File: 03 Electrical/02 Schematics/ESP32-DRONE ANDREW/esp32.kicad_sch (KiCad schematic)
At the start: 1 part, among them U1 ESP32-C3

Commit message: finished power managemnt
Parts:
- removed U1: ESP32-C3, Package_DFN_QFN:QFN-32-1EP_5x5mm_P0.5mm_EP3.7x3.7mm, symbol MCU_Espressif:ESP32-C3
- added C21: 1u, symbol Device:C_Small
- added L5: 39n, symbol Device:L_Small
- added P?: USB_C_Plug, symbol Connector:USB_C_Plug
- added R11: 0R0, symbol Device:R_Small
- added U5: ~, symbol Library 1:ESP32-PICO-V3
- added U?: CH340G, Package_SO:SOIC-16_3.9x9.9mm_P1.27mm, symbol Interface_USB:CH340G
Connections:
- new net: P?.A4 (VBUS), P?.A9 (VBUS), P?.B4 (VBUS), P?.B9 (VBUS)
- new net: P?.S1 (SHIELD), R11.1
- new net +3.3V: L5.1, U5.3 (VDDA3P3), U5.4 (VDDA3P3)
- new net GND1: C21.2, P?.A1 (GND), P?.A12 (GND), P?.B1 (GND), P?.B12 (GND), R11.2, U5.49 (GND)
- new net VDDA: C21.1, L5.2, U5.1 (VDDA), U5.46 (VDDA)
- no-connect marks 1 -> 4
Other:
- note removed: "No antenna required for the ESP32 will be using the LoRA module to communicate with our system"

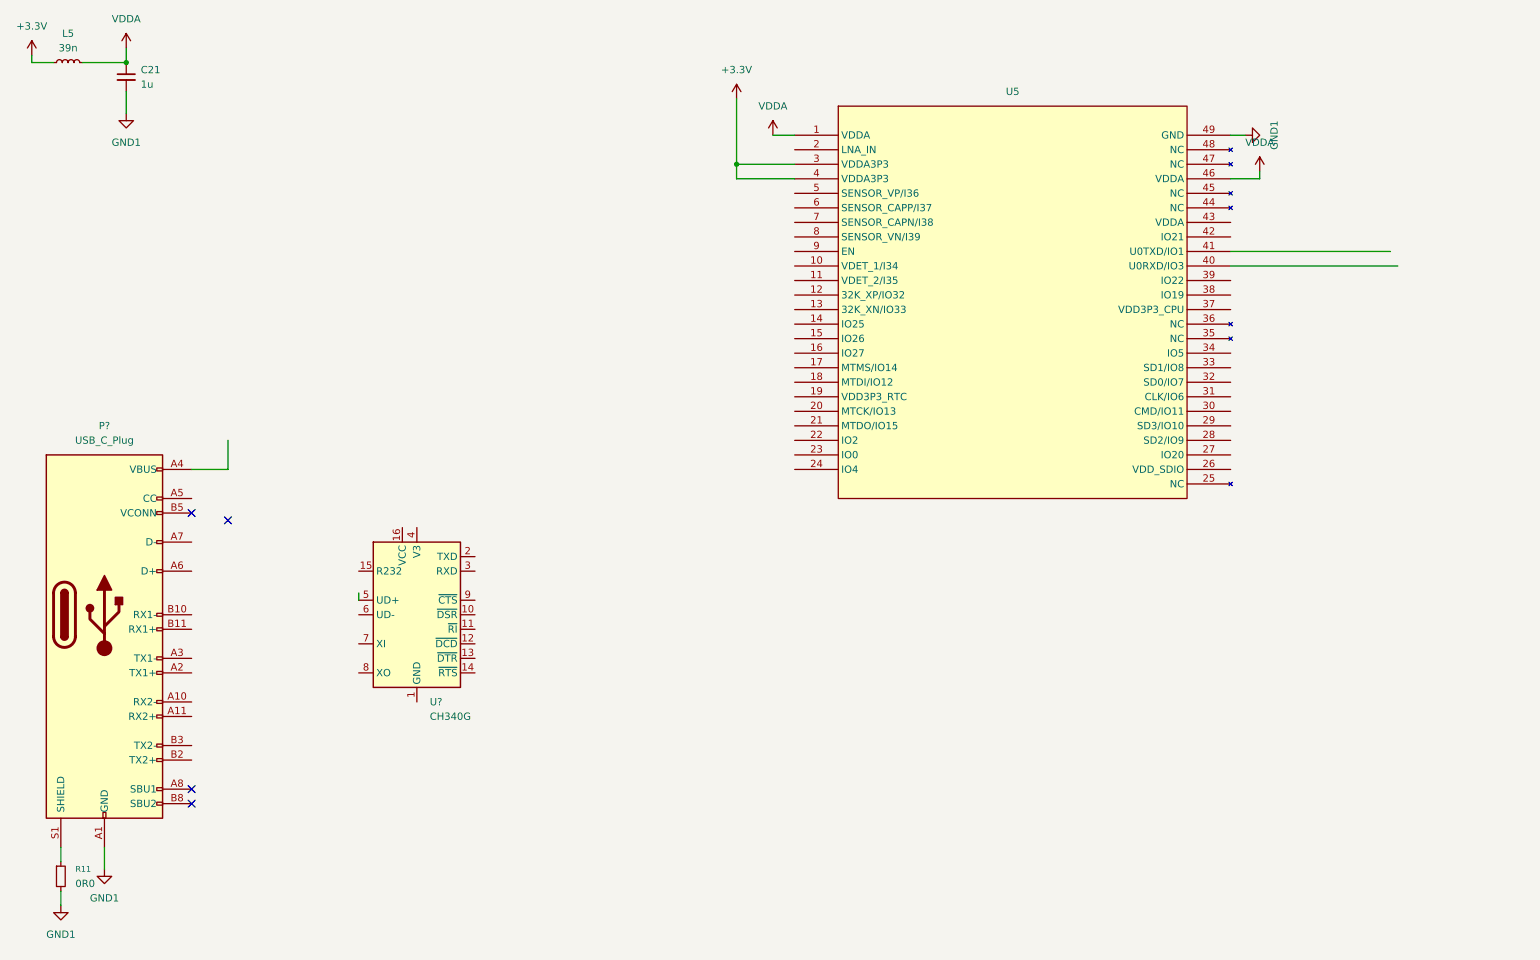
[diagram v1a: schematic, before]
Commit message: update 6/11
added the debugger circuit for the esp32 :
still missing the GPS circuit and the RF circuit
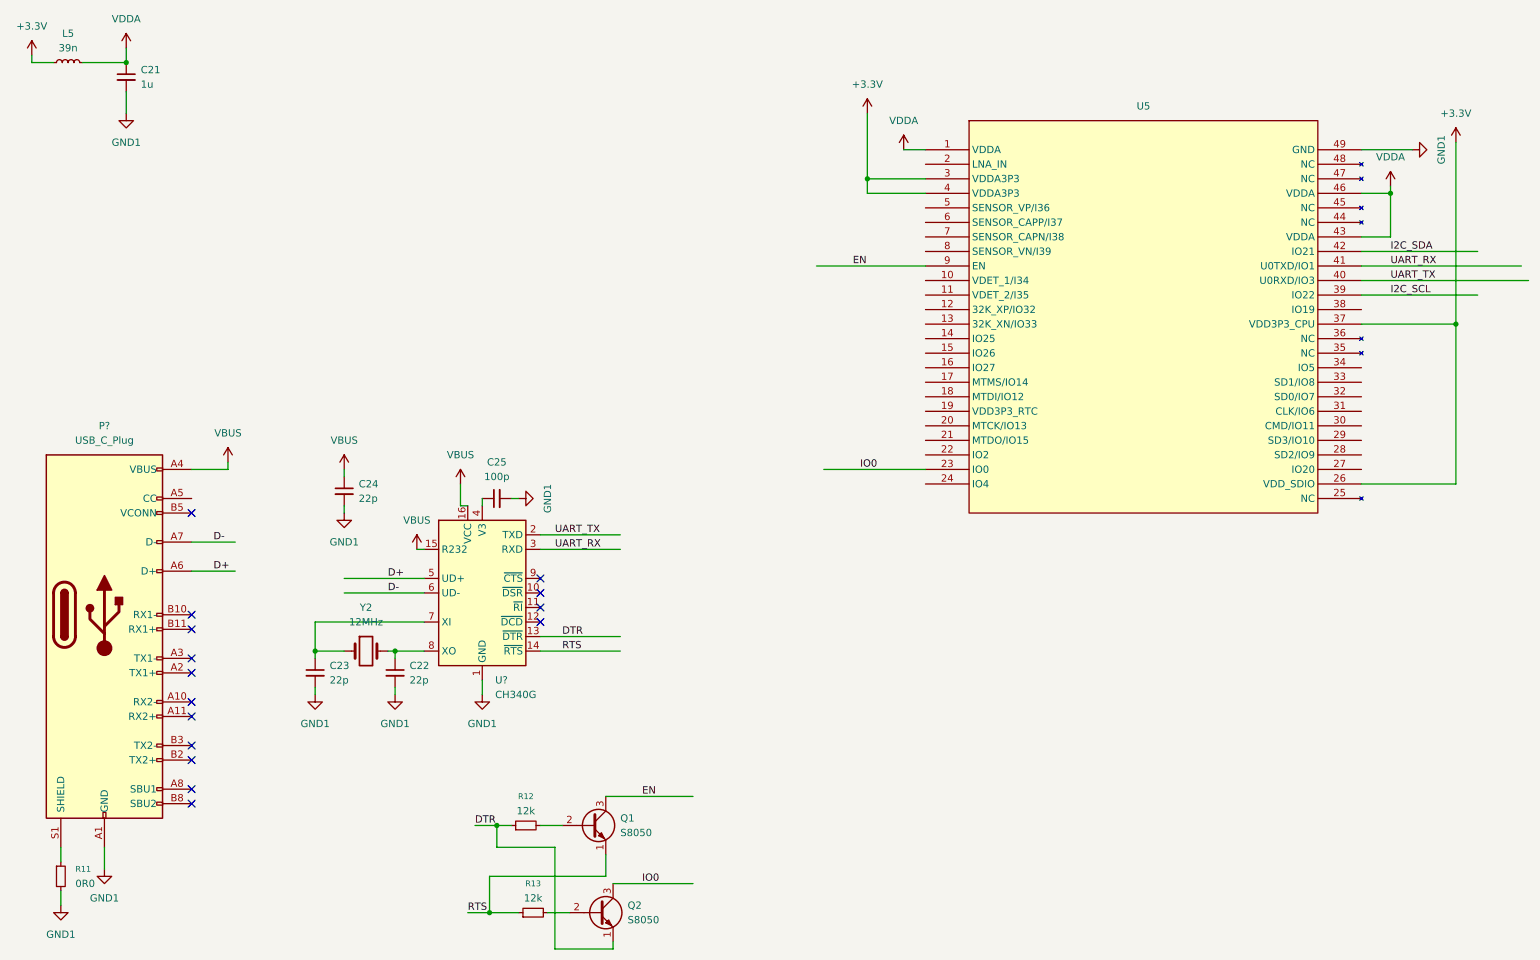
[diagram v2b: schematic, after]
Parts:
- added C22, C23, C24: 22p, symbol Device:C_Small
- added C25: 100p, symbol Device:C_Small
- added Q1, Q2: S8050, Package_TO_SOT_THT:TO-92_Inline, symbol Transistor_BJT:S8050
- added R12, R13: 12k, symbol Device:R_Small
- added Y2: 12MHz, symbol Device:Crystal
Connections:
- net +3.3V: now also U5.26 (VDD_SDIO), U5.37 (VDD3P3_CPU)
- net GND1: now also U?.1 (GND), C22.2, C23.2, C24.2, C25.2
- net VDDA: now also U5.43 (VDDA)
- net VBUS: now reaches P?.A4 (VBUS), P?.A9 (VBUS), P?.B4 (VBUS), P?.B9 (VBUS)
- net VBUS: now also U?.15 (R232), U?.16 (VCC), C24.1
- net D+: now reaches P?.A6 (D+)
- net D+: now also U?.5 (UD+)
- net D-: now reaches P?.A7 (D-)
- net D-: now also U?.6 (UD-)
- net IO0: now reaches U5.23 (IO0)
- net IO0: now also Q2.3 (C)
- net I2C_SCL: now reaches U5.39 (IO22)
- net UART_TX: now reaches U5.40 (U0RXD/IO3)
- net UART_TX: now also U?.2 (TXD)
- net UART_RX: now reaches U5.41 (U0TXD/IO1)
- net UART_RX: now also U?.3 (RXD)
- net I2C_SDA: now reaches U5.42 (IO21)
- net EN: now reaches U5.9 (EN)
- net EN: now also Q1.3 (C)
- net DTR: now reaches U?.13 (~{DTR})
- net DTR: now also Q2.1 (E), R12.1
- net RTS: now reaches U?.14 (~{RTS})
- net RTS: now also Q1.1 (E), R13.1
- net at U?.4 (V3): now also C25.1
- net at U?.7 (XI): now also C23.1, Y2.1
- net at U?.8 (XO): now also C22.1, Y2.2
- new net: Q1.2 (B), R12.2
- new net: Q2.2 (B), R13.2
- no-connect marks 4 -> 15
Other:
- moved on the sheet: U5, U?
